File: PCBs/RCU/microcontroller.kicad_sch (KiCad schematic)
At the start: 23 parts, among them J200 USB_C_Receptacle_USB2.0, J201 Conn_01x05, SW201 SW_Push, U200 STM32G0B1CBT6, Y200 Crystal

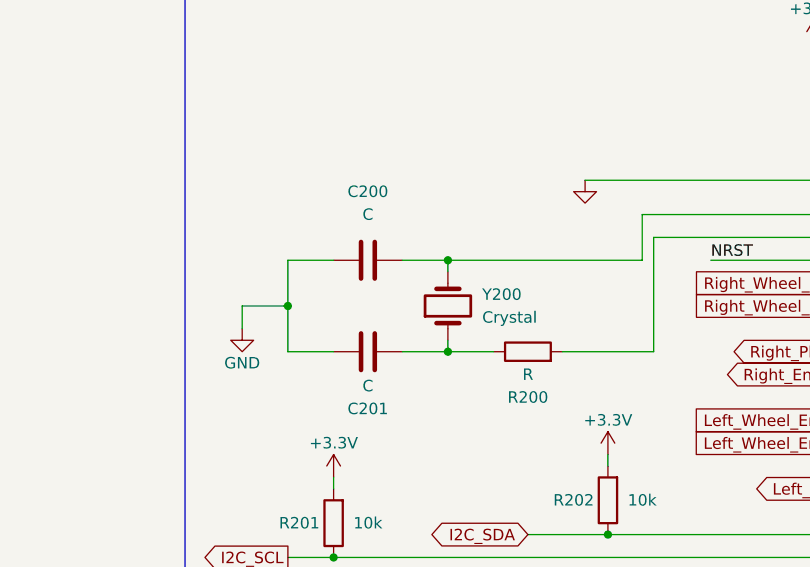
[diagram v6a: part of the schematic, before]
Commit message: Added 16Mhz crystal oscillator, along with load capacitors and external resistor
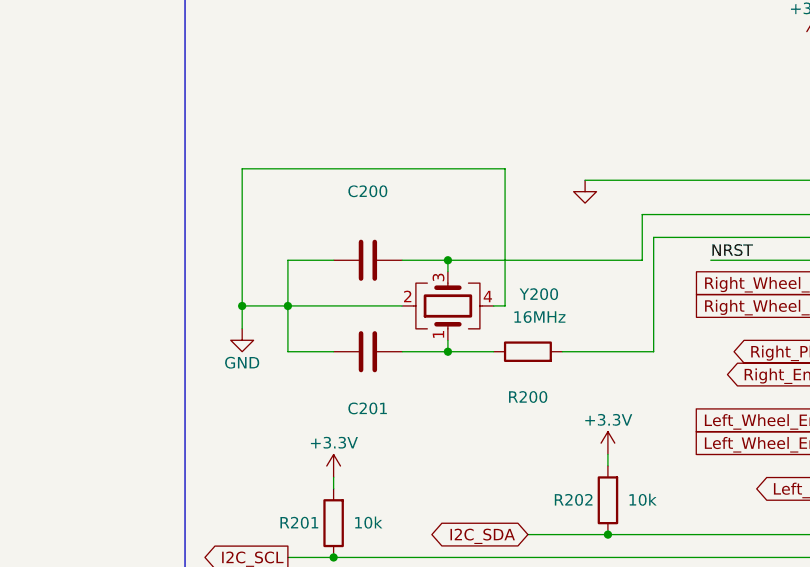
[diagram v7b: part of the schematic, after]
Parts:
- removed Y200: Crystal, symbol Device:Crystal
- added Y200: 16MHz, symbol Device:Crystal_GND24
- C200, C201: value C -> (none)
- R200: value R -> (none)
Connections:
- net GND: now also Y200.2, Y200.4
- net at C201.2, R200.1: now also Y200.1
- net at C200.1, U200.8 (PF0-OSC_IN): now also Y200.3
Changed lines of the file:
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@@
   (junction (at 224.79 142.24) (diameter 0) (color 0 0 0 0)
+  )
+  (junction (at 59.69 73.66) (diameter 0) (color 0 0 0 0)
   )
   (junction (at 214.63 156.21) (diameter 0) (color 0 0 0 0)
@@
     (stroke (width 0) (type default) (color 0 0 0 0))
   )
+  (wire (pts (xy 64.77 73.66) (xy 77.47 73.66))
+    (stroke (width 0) (type default) (color 0 0 0 0))
+  )
   (wire (pts (xy 64.77 78.74) (xy 69.85 78.74))
     (stroke (width 0) (type default) (color 0 0 0 0))
@@
     (stroke (width 0) (type default) (color 0 0 0 0))
   )
+  (wire (pts (xy 88.9 58.42) (xy 59.69 58.42))
+    (stroke (width 0) (type default) (color 0 0 0 0))
+  )
   (polyline (pts (xy 53.34 111.76) (xy 53.34 31.75))
     (stroke (width 0) (type default) (color 0 0 0 0))
@@
     (stroke (width 0) (type default) (color 0 0 0 0))
   )
+  (wire (pts (xy 88.9 73.66) (xy 88.9 58.42))
+    (stroke (width 0) (type default) (color 0 0 0 0))
+  )
   (wire (pts (xy 132.08 88.9) (xy 137.16 88.9))
     (stroke (width 0) (type default) (color 0 0 0 0))
@@
     (stroke (width 0) (type default) (color 0 0 0 0))
   )
+  (wire (pts (xy 59.69 58.42) (xy 59.69 73.66))
+    (stroke (width 0) (type default) (color 0 0 0 0))
+  )
   (wire (pts (xy 105.41 66.04) (xy 137.16 66.04))
     (stroke (width 0) (type default) (color 0 0 0 0))
@@
   )
   (wire (pts (xy 77.47 156.21) (xy 77.47 153.67))
+    (stroke (width 0) (type default) (color 0 0 0 0))
+  )
+  (wire (pts (xy 87.63 73.66) (xy 88.9 73.66))
     (stroke (width 0) (type default) (color 0 0 0 0))
   )
@@
     (in_bom yes) (on_board yes)
     (property "Reference" "C201" (id 0) (at 73.66 85.09 90))
-    (property "Value" "C" (id 1) (at 73.66 82.55 90))
+    (property "Value" "" (id 1) (at 73.66 82.55 90))
     (property "Footprint" "" (id 2) (at 77.47 77.7748 0)
       (effects (font (size 1.27 1.27)) hide)
@@
     (pin "1")
   )
+  (symbol (lib_id "Device:Crystal_GND24") (at 82.55 73.66 90) (unit 1)
+    (in_bom yes) (on_board yes)
+    (property "Reference" "Y200" (id 0) (at 92.71 72.39 90))
+    (property "Value" "16MHz" (id 1) (at 92.71 74.93 90))
+    (property "Footprint" "" (id 2) (at 82.55 73.66 0)
+      (effects (font (size 1.27 1.27)) hide)
+    )
+    (property "Datasheet" "~" (id 3) (at 82.55 73.66 0)
+      (effects (font (size 1.27 1.27)) hide)
+    )
+    (pin "1")
+    (pin "2")
+    (pin "3")
+    (pin "4")
+  )
   (symbol (lib_id "power:+3.3V") (at 100.33 90.17 0) (unit 1)
     (in_bom yes) (on_board yes)
@@
     )
     (property "Datasheet" "~" (id 3) (at 204.47 149.86 0)
-      (effects (font (size 1.27 1.27)) hide)
-    )
-    (pin "1")
-    (pin "2")
-  )
-  (symbol (lib_id "Device:Crystal") (at 82.55 73.66 90) (unit 1)
-    (in_bom yes) (on_board yes) (fields_autoplaced)
-    (property "Reference" "Y200" (id 0) (at 86.36 72.3899 90)
-      (effects (font (size 1.27 1.27)) (justify right))
-    )
-    (property "Value" "Crystal" (id 1) (at 86.36 74.9299 90)
-      (effects (font (size 1.27 1.27)) (justify right))
-    )
-    (property "Footprint" "" (id 2) (at 82.55 73.66 0)
-      (effects (font (size 1.27 1.27)) hide)
-    )
-    (property "Datasheet" "~" (id 3) (at 82.55 73.66 0)
       (effects (font (size 1.27 1.27)) hide)
     )
@@
     (in_bom yes) (on_board yes) (fields_autoplaced)
     (property "Reference" "C200" (id 0) (at 73.66 60.96 90))
-    (property "Value" "C" (id 1) (at 73.66 63.5 90))
+    (property "Value" "" (id 1) (at 73.66 63.5 90))
     (property "Footprint" "" (id 2) (at 69.85 69.5452 0)
       (effects (font (size 1.27 1.27)) hide)
@@
     (in_bom yes) (on_board yes)
     (property "Reference" "R200" (id 0) (at 91.44 83.82 90))
-    (property "Value" "R" (id 1) (at 91.44 81.28 90))
+    (property "Value" "" (id 1) (at 91.44 81.28 90))
     (property "Footprint" "" (id 2) (at 91.44 80.518 90)
       (effects (font (size 1.27 1.27)) hide)

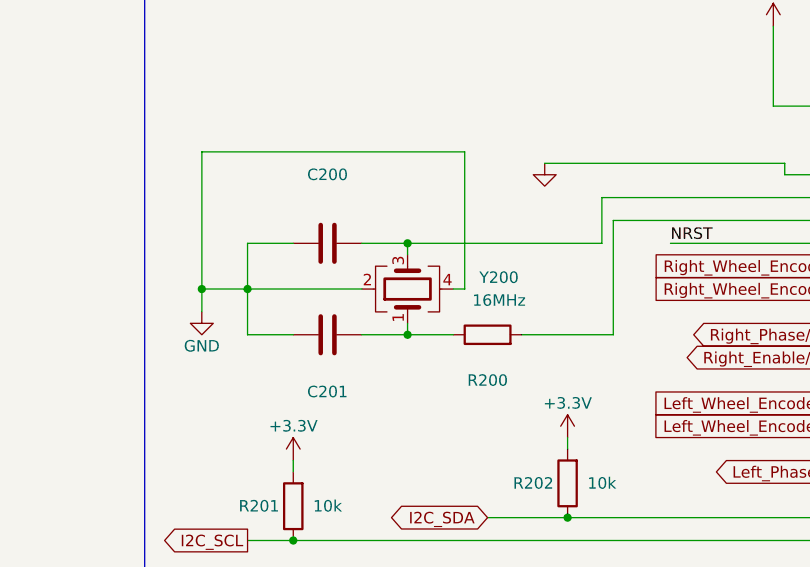
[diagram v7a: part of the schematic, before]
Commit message: Will use a 6V battery instead of 9V, since motor I am using is rated for 6V
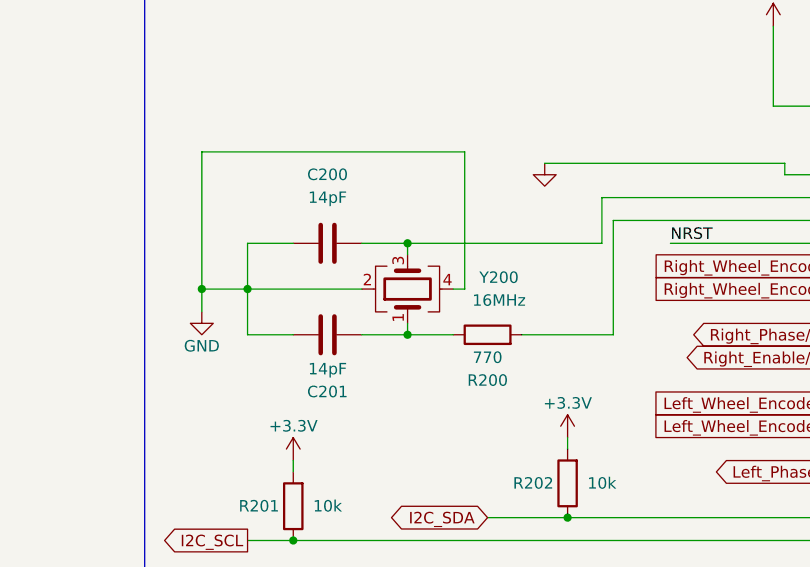
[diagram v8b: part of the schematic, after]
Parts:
- C200, C201: value (none) -> 14pF
- R200: value (none) -> 770
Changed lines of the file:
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@@
     (in_bom yes) (on_board yes)
     (property "Reference" "C201" (id 0) (at 73.66 85.09 90))
-    (property "Value" "" (id 1) (at 73.66 82.55 90))
+    (property "Value" "14pF" (id 1) (at 73.66 82.55 90))
     (property "Footprint" "" (id 2) (at 77.47 77.7748 0)
       (effects (font (size 1.27 1.27)) hide)
@@
     (in_bom yes) (on_board yes) (fields_autoplaced)
     (property "Reference" "C200" (id 0) (at 73.66 60.96 90))
-    (property "Value" "" (id 1) (at 73.66 63.5 90))
+    (property "Value" "14pF" (id 1) (at 73.66 63.5 90))
     (property "Footprint" "" (id 2) (at 69.85 69.5452 0)
       (effects (font (size 1.27 1.27)) hide)
@@
     (in_bom yes) (on_board yes)
     (property "Reference" "R200" (id 0) (at 91.44 83.82 90))
-    (property "Value" "" (id 1) (at 91.44 81.28 90))
+    (property "Value" "770" (id 1) (at 91.44 81.28 90))
     (property "Footprint" "" (id 2) (at 91.44 80.518 90)
       (effects (font (size 1.27 1.27)) hide)
